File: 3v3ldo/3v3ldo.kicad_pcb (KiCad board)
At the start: 2 copper layers, 3 parts, among them U101 NCP1117-3.3_SOT223

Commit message: update files to kicad 6
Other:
- net class Default removed

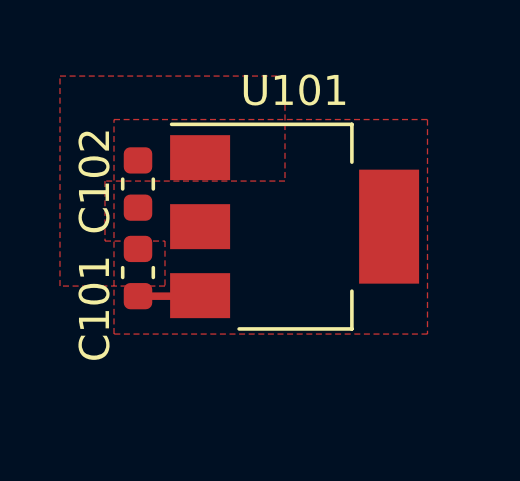
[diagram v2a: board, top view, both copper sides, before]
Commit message: delete kicad 6 dir
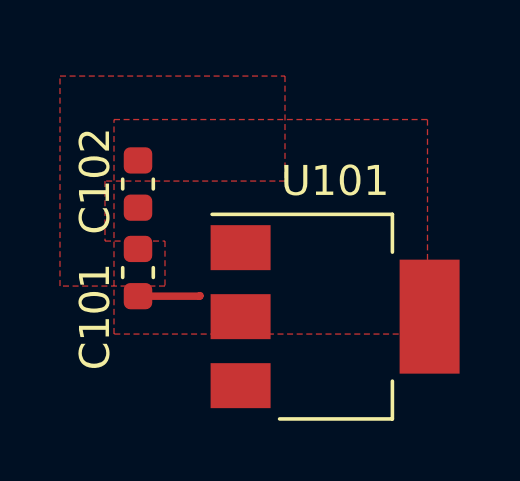
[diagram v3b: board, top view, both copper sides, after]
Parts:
- moved U101 3.29 mm to (144.2, 96.5)
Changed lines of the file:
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@@
     (tags "capacitor")
     (attr smd)
-    (fp_text reference "C101" (at -1.2 -1.43 90) (layer "F.SilkS")
+    (fp_text reference "C101" (at -1.47 -1.43 90) (layer "F.SilkS")
         (effects (font (size 1 1) (thickness 0.15)))
     )
@@
   )
   (footprint "Package_TO_SOT_SMD:SOT-223-3_TabPin2" (layer "F.Cu")
-    (at 142.82 93.52)
+    (at 144.17 96.52)
     (descr "module CMS SOT223 4 pins")
     (tags "CMS SOT")

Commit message: update LDO to kicad v7 format
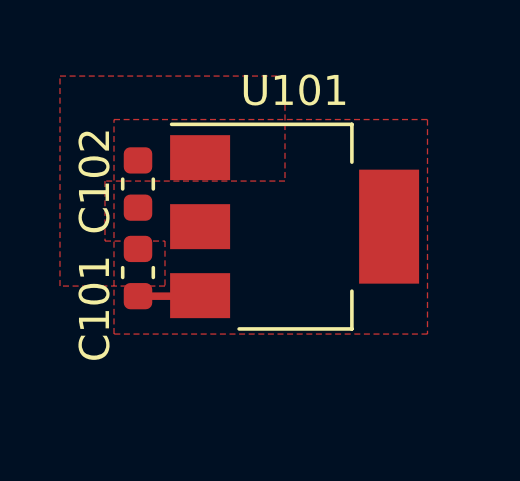
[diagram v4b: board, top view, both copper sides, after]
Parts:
- moved U101 3.29 mm to (142.8, 93.5)
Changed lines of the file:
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@@
     (tags "capacitor")
     (attr smd)
-    (fp_text reference "C101" (at -1.47 -1.43 90) (layer "F.SilkS")
+    (fp_text reference "C101" (at -1.2 -1.43 90) (layer "F.SilkS")
         (effects (font (size 1 1) (thickness 0.15)))
     )
@@
   )
   (footprint "Package_TO_SOT_SMD:SOT-223-3_TabPin2" (layer "F.Cu")
-    (at 144.17 96.52)
+    (at 142.82 93.52)
     (descr "module CMS SOT223 4 pins")
     (tags "CMS SOT")
